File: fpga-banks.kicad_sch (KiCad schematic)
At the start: 9 parts, among them U1 XC7K70T-FBG484, U2 ASFLMB-100.000MHZ-XY-T

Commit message: Fix issues after returning from local branch
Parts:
- added U?: AMJMEFB-100.0000T, antmicro-footprints:AMJMEFB, symbol antmicroOscillators:AMJMEFB-100.0000T
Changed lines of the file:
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@@
     (pin "1")
   )
+  (symbol (lib_id "antmicroOscillators:AMJMEFB-100.0000T") (at 115.57 231.14 0) (unit 1)
+    (in_bom yes) (on_board yes) (fields_autoplaced)
+    (property "Reference" "U?" (id 0) (at 131.445 224.5159 0)
+      (effects (font (size 1.524 1.524)))
+    )
+    (property "Value" "AMJMEFB-100.0000T" (id 1) (at 131.445 227.5093 0)
+      (effects (font (size 1.524 1.524)))
+    )
+    (property "Footprint" "antmicro-footprints:AMJMEFB" (id 2) (at 135.89 225.044 0)
+      (effects (font (size 1.524 1.524)) hide)
+    )
+    (property "Datasheet" "" (id 3) (at 115.57 231.14 0)
+      (effects (font (size 1.524 1.524)))
+    )
+    (property "MPN" "AMJMEFB-100.0000T" (id 4) (at 115.57 231.14 0)
+      (effects (font (size 1.27 1.27)) hide)
+    )
+    (property "Field5" "Abracon" (id 5) (at 115.57 231.14 0)
+      (effects (font (size 1.27 1.27)) hide)
+    )
+    (pin "1")
+    (pin "2")
+    (pin "3")
+    (pin "4")
+  )
 )

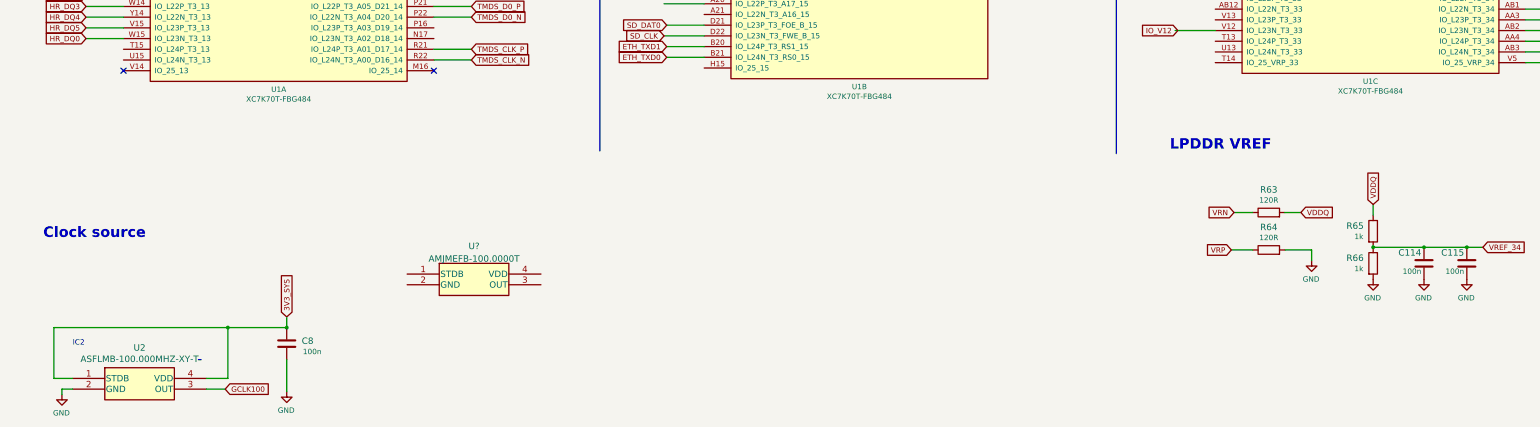
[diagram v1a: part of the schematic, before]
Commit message: Placement and routing of FT4232H. Re annotation of the schematics
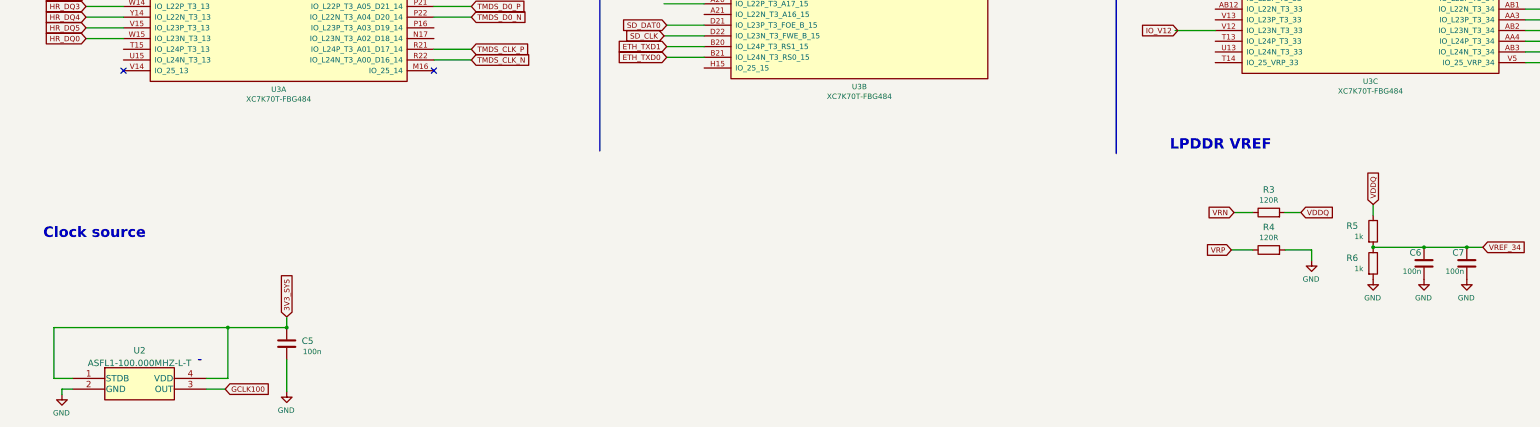
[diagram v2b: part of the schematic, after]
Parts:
- removed U2: ASFLMB-100.000MHZ-XY-T, lpddr4-test-board-footprints:ASFLMB-100.000MHZ-XY-T, symbol lpddr4-test-board:ASFLMB-100.000MHZ-XY-T
- removed U?: AMJMEFB-100.0000T, antmicro-footprints:AMJMEFB, symbol antmicroOscillators:AMJMEFB-100.0000T
- added U2: ASFL1-100.000MHZ-L-T, antmicro-footprints:Oscillator_SMD_Abracon_ASFL1-4Pin_5.0x3.2mm, symbol antmicroOscillators:ASFL1-100.000MHZ-L-T
- renumbered C8 to C5, C114 to C6, C115 to C7, R63 to R3, R64 to R4, R65 to R5, R66 to R6, U1 to U3
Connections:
- net 3V3_SYS: now also U2.1 (STDB), U2.4 (VDD)
- net GCLK100: now also U2.3 (OUT)
- net GND: now also U2.2 (GND)
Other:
- note removed: "IC2"
